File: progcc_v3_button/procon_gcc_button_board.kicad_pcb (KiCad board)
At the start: 2 copper layers, 110 x 54.3 mm, 31 parts, among them J1 Button Board, J2 bumpers, SW1 procon_abxy, SW2 procon_dpad, SW3 TL3315NF100Q, SW4 TL3315NF100Q, SW5 TL3315NF100Q, SW6 TL3315NF100Q

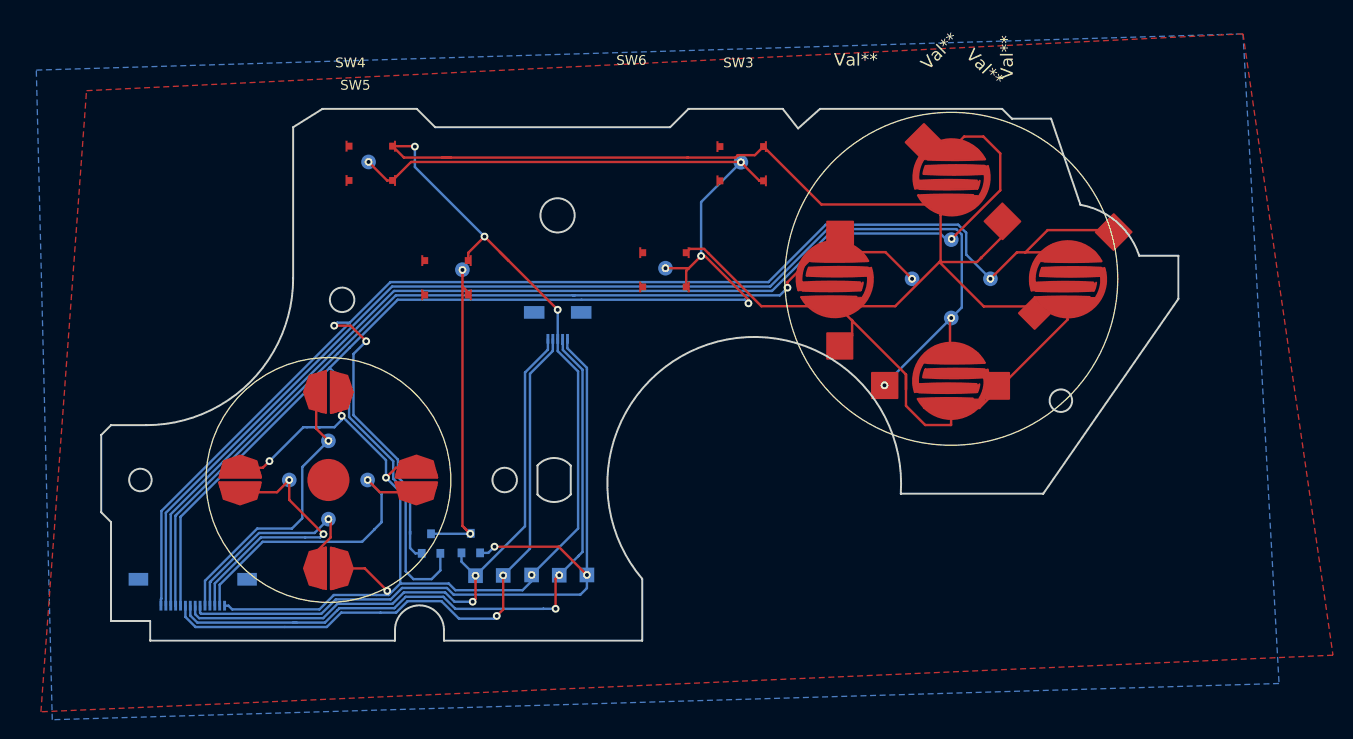
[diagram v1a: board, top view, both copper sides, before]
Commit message: Update button board
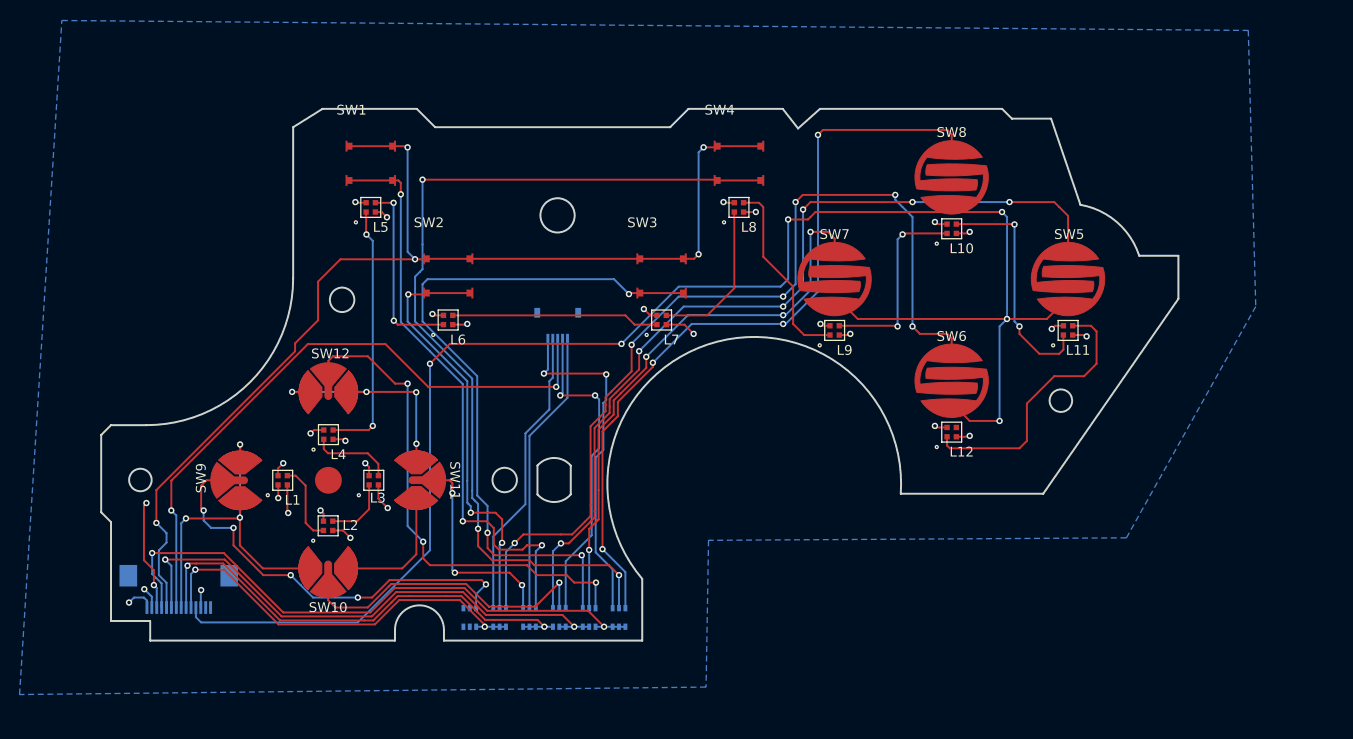
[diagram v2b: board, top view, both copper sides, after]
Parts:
- removed Ref** (x4): Val**, procon_gcc:ABXY_Contact_Omron_Switch
- removed the SW1 at (166.0, 44.7)
- removed the SW2 at (102.4, 65.2)
- removed TP1, TP10, TP11, TP12, TP13, TP14, TP2, TP3, TP4, TP5 (x4), TP6, TP7, TP8, TP9: TestPoint, TestPoint:TestPoint_Pad_D1.5mm
- added D3: BAS16VY,115, Package_TO_SOT_SMD:SOT-363_SC-70-6, B.Cu at (126.0, 79.2)
- added D4: BAS16VY,115, Package_TO_SOT_SMD:SOT-363_SC-70-6, B.Cu at (122.9, 79.2)
- added D5: BAS16VY,115, Package_TO_SOT_SMD:SOT-363_SC-70-6, B.Cu at (119.9, 79.2)
- added D6: BAS16VY,115, Package_TO_SOT_SMD:SOT-363_SC-70-6, B.Cu at (116.8, 79.2)
- added L1: SK6805-EC-15, progcc_v3:SK6805-EC-15, F.Cu at (97.7, 65.2)
- added L10: SK6805-EC-15, progcc_v3:SK6805-EC-15, F.Cu at (166.1, 39.6)
- added L11: SK6805-EC-15, progcc_v3:SK6805-EC-15, F.Cu at (177.9, 49.9)
- added L12: SK6805-EC-15, progcc_v3:SK6805-EC-15, F.Cu at (166.1, 60.3)
- added L2: SK6805-EC-15, progcc_v3:SK6805-EC-15, F.Cu at (102.4, 69.9)
- added L3: SK6805-EC-15, progcc_v3:SK6805-EC-15, F.Cu at (107.0, 65.2)
- added L4: SK6805-EC-15, progcc_v3:SK6805-EC-15, F.Cu at (102.4, 60.6)
- added L5: SK6805-EC-15, progcc_v3:SK6805-EC-15, F.Cu at (106.7, 37.4)
- added L6: SK6805-EC-15, progcc_v3:SK6805-EC-15, F.Cu at (114.6, 48.9)
- added L7: SK6805-EC-15, progcc_v3:SK6805-EC-15, F.Cu at (136.4, 48.9)
- added L8: SK6805-EC-15, progcc_v3:SK6805-EC-15, F.Cu at (144.3, 37.4)
- added L9: SK6805-EC-15, progcc_v3:SK6805-EC-15, F.Cu at (154.1, 49.9)
- added SW10: DPAD, progcc_v3:progcc_dpad, F.Cu at (102.4, 74.2)
- added SW11: DPAD, progcc_v3:progcc_dpad, F.Cu at (111.4, 65.2)
- added SW12: DPAD, progcc_v3:progcc_dpad, F.Cu at (102.4, 56.2)
- added SW5: BPAD, progcc_v3:progcc_bpad, F.Cu at (177.9, 44.7)
- added SW6: BPAD, progcc_v3:progcc_bpad, F.Cu at (166.1, 55.1)
- added SW7: BPAD, progcc_v3:progcc_bpad, F.Cu at (154.1, 44.7)
- added SW8: BPAD, progcc_v3:progcc_bpad, F.Cu at (166.1, 34.3)
- added SW9: DPAD, progcc_v3:progcc_dpad, F.Cu at (93.4, 65.2)
- D1, D2: value BAV70 -> BAS16VY,115; footprint Package_TO_SOT_SMD:SOT-23 -> Package_TO_SOT_SMD:SOT-363_SC-70-6
- J1: value Button Board -> To Button Board; footprint procon_gcc:molex_5051101492_14P -> progcc_v3:molex_5051101492_14P
- J2: footprint procon_gcc:molex_5051100592_5P -> progcc_v3:molex_5051100592_5P
- SW1: renamed from SW5; footprint procon_gcc:TL3315NFxxxQ -> progcc_v3:TL3315NFxxxQ
- SW2: renamed from SW4; footprint procon_gcc:TL3315NFxxxQ -> progcc_v3:TL3315NFxxxQ
- SW3: renamed from SW6; footprint procon_gcc:TL3315NFxxxQ -> progcc_v3:TL3315NFxxxQ
- SW4: renamed from SW3; footprint procon_gcc:TL3315NFxxxQ -> progcc_v3:TL3315NFxxxQ
- moved D2 17.8 mm to (129.0, 79.2)
- moved D1 16.9 mm to (132.1, 79.2)
- moved J1 3.56 mm to (87.1, 75.0)
- moved J2 1.90 mm to (125.8, 49.2)
- moved SW3 0.69 mm to (134.2, 42.6)
- moved SW4 0.28 mm to (142.1, 31.1)
- moved SW2 0.25 mm to (112.4, 42.6)
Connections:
- D1 pad 1: BB_BTN_RT -> Push_A
- D1 pad 2: BB_BTN_LT -> Push_A
- D1 pad 3: Net-(D1-Pad3) -> Push_A
- D2 pad 1: BB_BTN_ST -> Push_A
- D2 pad 2: BB_BTN_A -> Push_B
- D2 pad 3: Net-(D1-Pad3) -> Push_B
- J1 pad 1: BB_BTN_A -> GND
- J1 pad 10: BB_BTN_DP_U -> Push_D
- J1 pad 11: BB_BTN_DP_D -> Scan_A
- J1 pad 12: BB_BTN_DP_L -> GND
- J1 pad 13: BB_BTN_DP_R -> NFC
- J1 pad 14: GND -> NFC
- J1 pad 2: BB_BTN_B -> +3V3
- J1 pad 3: BB_BTN_X -> BUTTON_RGB
- J1 pad 4: BB_BTN_Y -> Push_A
- J1 pad 5: BB_BTN_ST -> Scan_C
- J1 pad 6: BB_BTN_ZL -> Push_B
- J1 pad 7: BB_BTN_ZR -> Scan_D
- J1 pad 8: BB_BTN_LT -> Scan_B
- J1 pad 9: BB_BTN_RT -> Push_C
- J2 pad 1: BB_BTN_LT -> ZL_Pull
- J2 pad 2: BB_BTN_ZL -> L_Pull
- J2 pad 3: GND -> Scan_D
- J2 pad 4: BB_BTN_ZR -> R_Pull
- J2 pad 5: BB_BTN_RT -> ZR_Pull
- SW1 pad 1: BB_BTN_ST -> Scan_C
- SW1 pad 2: GND -> Scan_C
- SW1 pad 3: (no net) -> Minus_Pull
- SW1 pad 4: (no net) -> Minus_Pull
- SW2 pad 1: Net-(D1-Pad3) -> Scan_C
- SW2 pad 2: GND -> Scan_C
- SW2 pad 3: (no net) -> Capture_Pull
- SW2 pad 4: (no net) -> Capture_Pull
- SW3 pad 1: BB_BTN_ST -> Scan_C
- SW3 pad 2: GND -> Scan_C
- SW3 pad 3: (no net) -> Home_Pull
- SW3 pad 4: (no net) -> Home_Pull
- SW4 pad 1: BB_BTN_ST -> Scan_C
- SW4 pad 2: GND -> Scan_C
- SW4 pad 3: (no net) -> Plus_Pull
- SW4 pad 4: (no net) -> Plus_Pull
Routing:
- net GND: track 304.9 -> 20.4 mm, vias 8 -> 14
- net BB_BTN_ST: track 173.7 -> 0.00 mm, vias 5 -> 0
- net Scan_A: track 0.00 -> 168.4 mm, vias 0 -> 6
- net BB_BTN_A: track 160.0 -> 0.00 mm, vias 3 -> 0
- net BB_BTN_B: track 125.4 -> 0.00 mm, vias 2 -> 0
- net BB_BTN_X: track 118.5 -> 0.00 mm, vias 1 -> 0
- net Scan_C: track 0.00 -> 116.0 mm, vias 0 -> 5
- net BB_BTN_Y: track 97.3 -> 0.00 mm, vias 2 -> 0
- net Plus_Pull: track 0.00 -> 94.0 mm, vias 0 -> 3
- net B_Pull: track 0.00 -> 93.6 mm, vias 0 -> 6
- net A_Pull: track 0.00 -> 89.4 mm, vias 0 -> 6
- net BB_BTN_RT: track 80.6 -> 0.00 mm, vias 2 -> 0
- net X_Pull: track 0.00 -> 79.7 mm, vias 0 -> 4
- net Home_Pull: track 0.00 -> 72.6 mm, vias 0 -> 3
- net Scan_B: track 0.00 -> 72.0 mm, vias 0 -> 7
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- added copper zone on In2.Cu, net +3V3
- added copper zone on B.Cu, net GND
- added copper zone on In1.Cu, net GND
- removed copper zone on B.Cu, net (none)
- removed copper zone on F.Cu, net (none)
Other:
- copper layers 2 -> 4
- board text removed: "A"
- board text removed: "B"
- board text removed: "DP_D"
- board text removed: "DP_L"
- board text removed: "DP_R"
- board text removed: "DP_U"
- board text removed: "GND"
- board text removed: "L+R+A+ST"
- board text removed: "LT"
- board text removed: "RT"
- board text removed: "ST"
- board text removed: "X"
- board text removed: "Y"
- board text removed: "ZL"
- board text removed: "ZR"

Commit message: Update Pads and DRC
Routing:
- net Scan_B: track 72.0 -> 90.0 mm, vias 7 -> 10
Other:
- rule solder_mask_min_width: 0.25 -> 0.15

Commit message: Production files
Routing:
- net GND: vias 14 -> 29
- added copper zone on F.Cu, net GND
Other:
- rule pad_to_mask_clearance: 0.051 -> 0

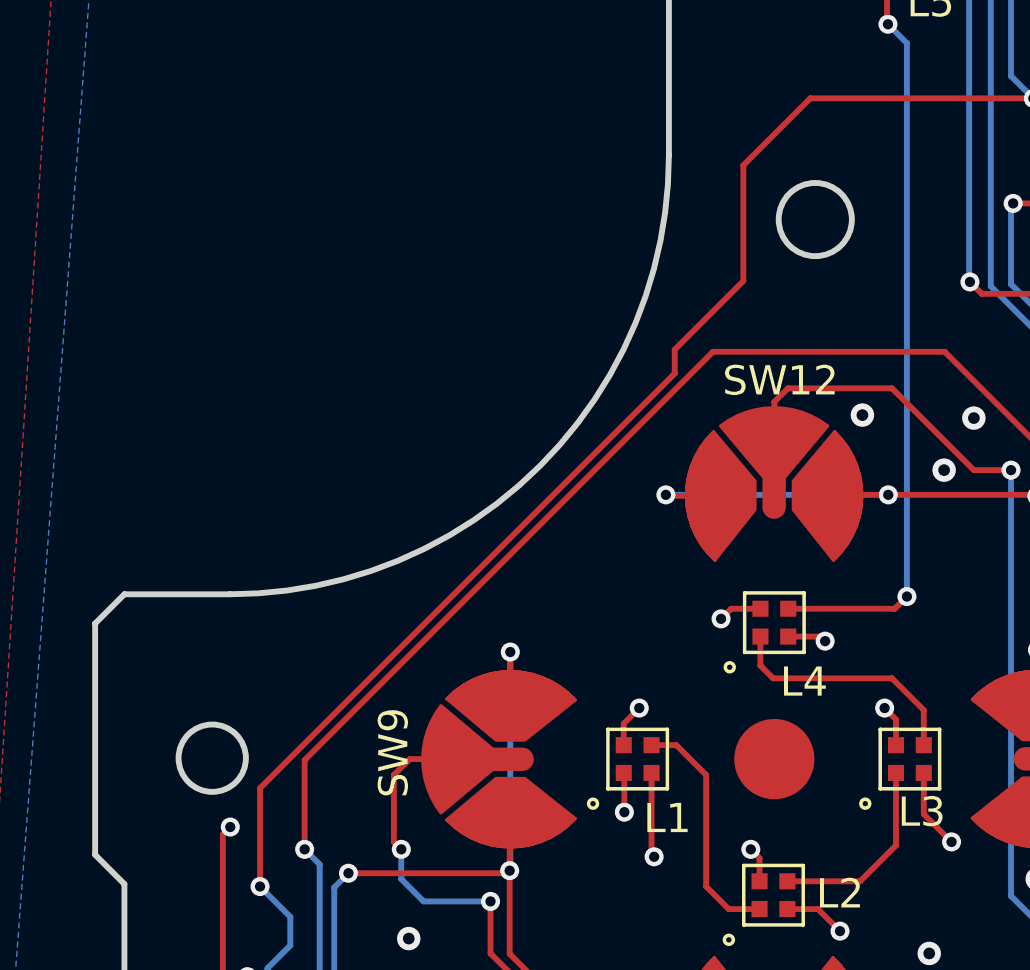
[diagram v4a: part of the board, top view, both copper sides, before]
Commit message: Update proto
- Update stick position
- Adjust some screw position slightly
- Fix schematic for Crystal and Rumble
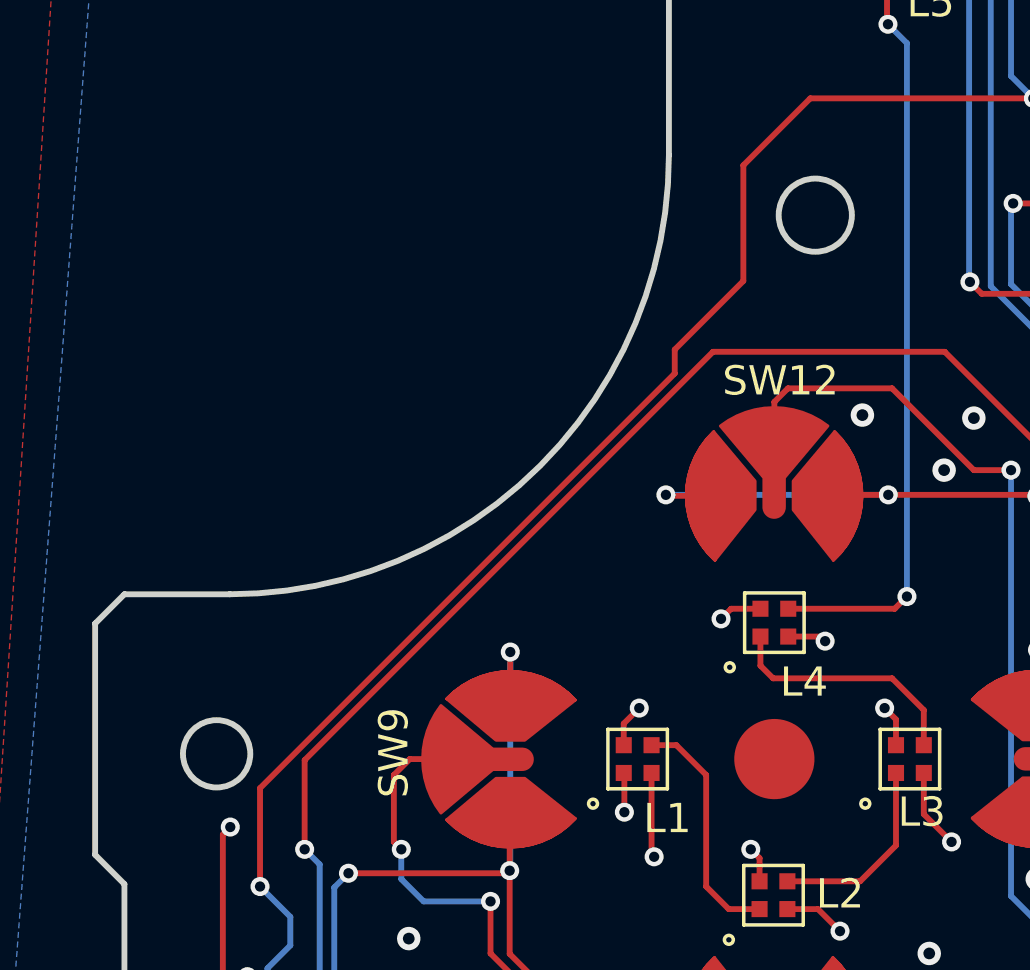
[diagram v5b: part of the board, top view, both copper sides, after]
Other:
- outline, holes or cut-outs redrawn
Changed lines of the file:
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@@
   (gr_line (start 148.803279 27.312388) (end 150.367211 29.312388)
     (stroke (width 0.2) (type solid)) (layer "Edge.Cuts"))
-  (gr_circle (center 103.80328 46.812389) (end 103.80328 48.062389)
+  (gr_circle (center 103.80328 46.662389) (end 105.05328 46.662389)
     (stroke (width 0.2) (type solid)) (fill none) (layer "Edge.Cuts"))
   (gr_line (start 150.367211 29.312388) (end 152.603279 27.312388)
@@
   (gr_line (start 172.203279 28.312388) (end 176.203279 28.312388)
     (stroke (width 0.2) (type solid)) (layer "Edge.Cuts"))
-  (gr_circle (center 83.20328 65.212387) (end 83.20328 66.362387)
+  (gr_circle (center 83.35328 65.062387) (end 84.50328 65.062387)
     (stroke (width 0.2) (type solid)) (fill none) (layer "Edge.Cuts"))
   (gr_line (start 171.203279 27.312388) (end 152.603279 27.312388)
